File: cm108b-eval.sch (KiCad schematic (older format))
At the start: 44 parts, among them IC1 CM108B, J1 SPKR, J2 MIC, J3 RADIO_DATA, SW1 MUTE_REC, SW2 MUTE_PLAY, SW3 VOL_DN, SW4 VOL_UP

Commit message: Fix R and L on J1
Resolves #1
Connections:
- net AUDIO_L: now also J1.T; no longer J1.R
- net AUDIO_R: now also J1.R; no longer J1.T
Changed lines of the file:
@@
 Sheet 1 1
 Title "CM108B Evaluation Board"
-Date "2021-04-18"
-Rev "4"
+Date "2021-04-21"
+Rev "5"
 Comp "Chris Keller"
 Comment1 "Licensed under Creative Commons CC-BY-4.0"
@@
 Text Label 8650 4450 2    50   ~ 0
 MIC_BIAS
+Text Label 8650 3850 2    50   ~ 0
+AUDIO_L
 Text Label 8650 3950 2    50   ~ 0
-AUDIO_L
-Text Label 8650 3850 2    50   ~ 0
 AUDIO_R
 Text Label 9350 3050 2    50   ~ 0

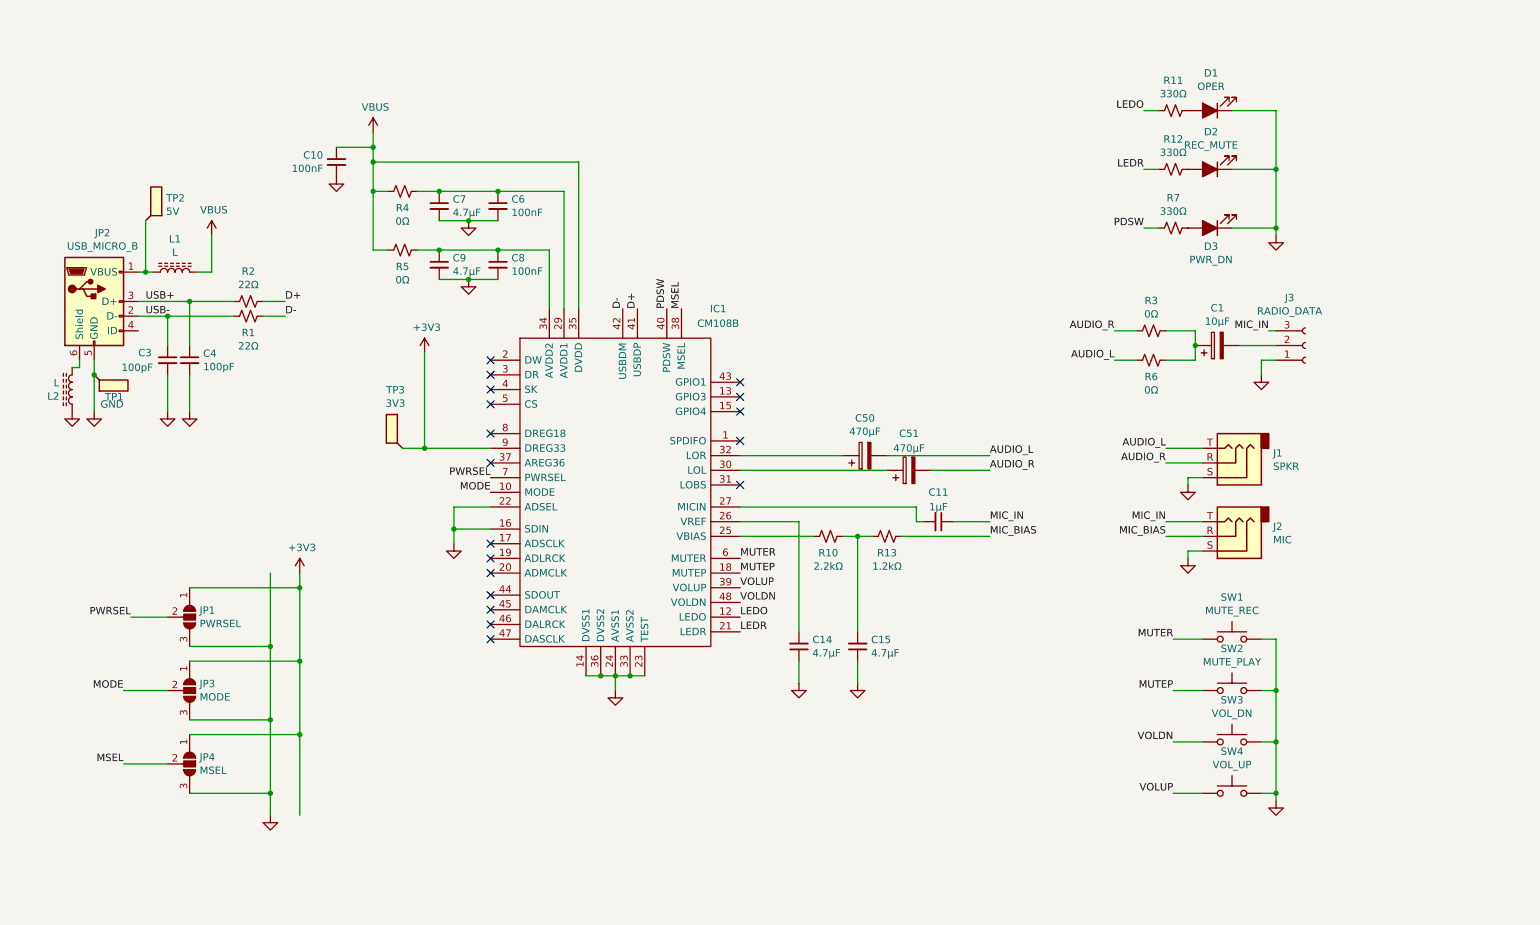
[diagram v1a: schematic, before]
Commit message: Copy from HS100B project to get identical layouts
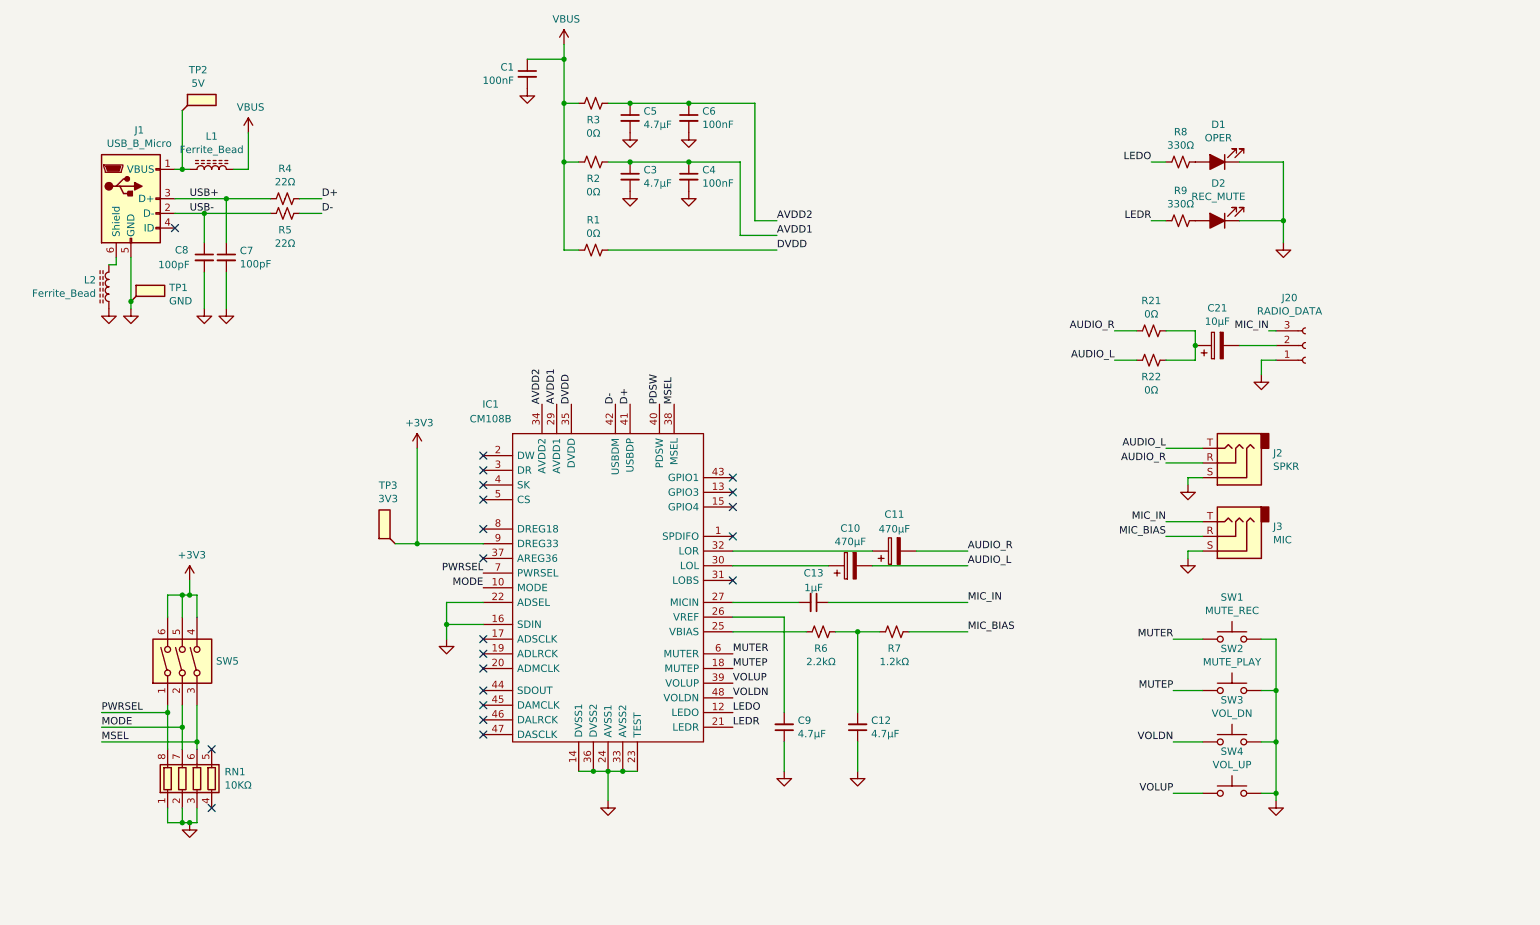
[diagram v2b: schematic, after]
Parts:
- removed D3: PWR_DN, LED_SMD:LED_0603_1608Metric, symbol Device:LED_ALT
- removed IC1: CM108B, Package_QFP:LQFP-48_7x7mm_P0.5mm, symbol CM108:CM108
- removed JP1: PWRSEL, Connector_PinHeader_2.54mm:PinHeader_1x03_P2.54mm_Vertical, symbol Jumper:SolderJumper_3_Open
- removed JP2: USB_MICRO_B, CUI:UJ2-MIBH-4-SMT, symbol Connector:USB_B_Micro
- removed JP3: MODE, Connector_PinHeader_2.54mm:PinHeader_1x03_P2.54mm_Vertical, symbol Jumper:SolderJumper_3_Open
- removed JP4: MSEL, Connector_PinHeader_2.54mm:PinHeader_1x03_P2.54mm_Vertical, symbol Jumper:SolderJumper_3_Open
- removed R7: 330Ω, Resistor_SMD:R_1210_3225Metric, symbol Device:R_Small_US
- added IC1: CM108B, Package_QFP:LQFP-48_7x7mm_P0.5mm, symbol CM108:CM108B
- added J1: USB_B_Micro, CUI:UJ2-MIBH-4-SMT, symbol Connector:USB_B_Micro
- added R1: 0Ω, Resistor_SMD:R_1210_3225Metric, symbol Device:R_Small_US
- added RN1: 10KΩ, Resistor_SMD:R_Array_Concave_4x0402, symbol Device:R_Pack04
- added SW5: SW_DIP_x03, Wurth:416131160803, symbol Switch:SW_DIP_x03
- L1, L2: value L -> Ferrite_Bead
- renumbered C10 to C1, C50 to C10, C51 to C11, C15 to C12, C11 to C13, C1 to C21, C9 to C3, C8 to C4, C7 to C5, C4 to C7, C3 to C8, C14 to C9, J1 to J2, J3 to J20, J2 to J3, R5 to R2, R3 to R21, R6 to R22, R4 to R3, R2 to R4, R1 to R5, R10 to R6, R13 to R7, R11 to R8, R12 to R9
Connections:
- net +3V3: now also IC1.9 (DREG33), SW5.4, SW5.5, SW5.6
- net D+: now also IC1.41 (USBDP)
- net D-: now also IC1.42 (USBDM)
- net GND: now also IC1.14 (DVSS1), IC1.16 (SDIN), IC1.22 (ADSEL), IC1.23 (TEST), IC1.24 (AVSS1), IC1.33 (AVSS2), IC1.36 (DVSS2), J1.5 (GND), RN1.1 (R1.1), RN1.2 (R2.1), RN1.3 (R3.1)
- net LEDO: now also IC1.12 (LEDO)
- net LEDR: now also IC1.21 (LEDR)
- net MODE: now also IC1.10 (MODE), RN1.7 (R2.2), SW5.2
- net MSEL: now also IC1.38 (MSEL), RN1.6 (R3.2), SW5.3
- net MUTEP: now also IC1.18 (MUTEP)
- net MUTER: now also IC1.6 (MUTER)
- net PDSW: now also IC1.40 (PDSW)
- net PWRSEL: now also IC1.7 (PWRSEL), RN1.8 (R1.2), SW5.1
- net USB+: now also J1.3 (D+)
- net USB-: now also J1.2 (D-)
- net VBUS: now also R1.2
- net VOLDN: now also IC1.48 (VOLDN)
- net VOLUP: now also IC1.39 (VOLUP)
- net at R6.2: now also IC1.25 (VBIAS)
- net at C9.2: now also IC1.26 (VREF)
- net at C13.2: now also IC1.27 (MICIN)
- net AVDD2: now reaches C5.1, C6.1, R3.1
- net AVDD2: now also IC1.34 (AVDD2)
- net at C11.1: now also IC1.32 (LOR)
- net at C10.1: now also IC1.30 (LOL)
- net AVDD1: now reaches C3.1, C4.1, R2.1
- net AVDD1: now also IC1.29 (AVDD1)
- net at L1.1, TP2.1: now also J1.1 (VBUS)
- net at L2.2: now also J1.6 (Shield)
- new net DVDD: IC1.35 (DVDD), R1.1
- no-connect marks 18 -> 21
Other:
- moved on the sheet: C1, C10, C11, C12, C13, C3, C4, C5, C6, C7, C8, C9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

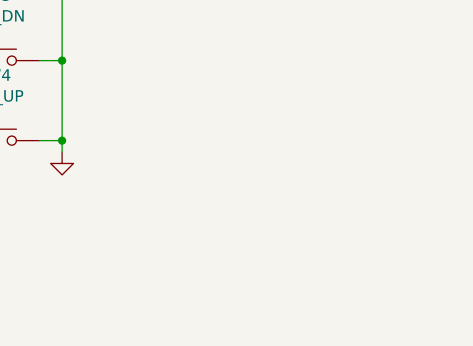
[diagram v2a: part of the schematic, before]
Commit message: Add OSHW logo
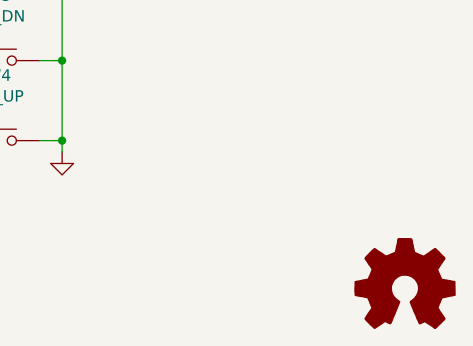
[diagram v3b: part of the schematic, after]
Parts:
- added LOGO1: Logo_Open_Hardware_Small, Symbol:OSHW-Logo2_9.8x8mm_SilkScreen, symbol Graphic:Logo_Open_Hardware_Small
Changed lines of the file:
@@
 	3750 4900 3750 5050
 Connection ~ 3750 5050
+$Comp
+L Graphic:Logo_Open_Hardware_Small LOGO1
+U 1 1 6086348C
+P 10900 6850
+F 0 "LOGO1" H 10900 7125 50  0001 C CNN
+F 1 "Logo_Open_Hardware_Small" H 10900 6625 50  0001 C CNN
+F 2 "Symbol:OSHW-Logo2_9.8x8mm_SilkScreen" H 10900 6850 50  0001 C CNN
+F 3 "~" H 10900 6850 50  0001 C CNN
+	1    10900 6850
+	1    0    0    -1
+$EndComp
 $EndSCHEMATC
